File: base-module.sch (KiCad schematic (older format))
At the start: 0 parts

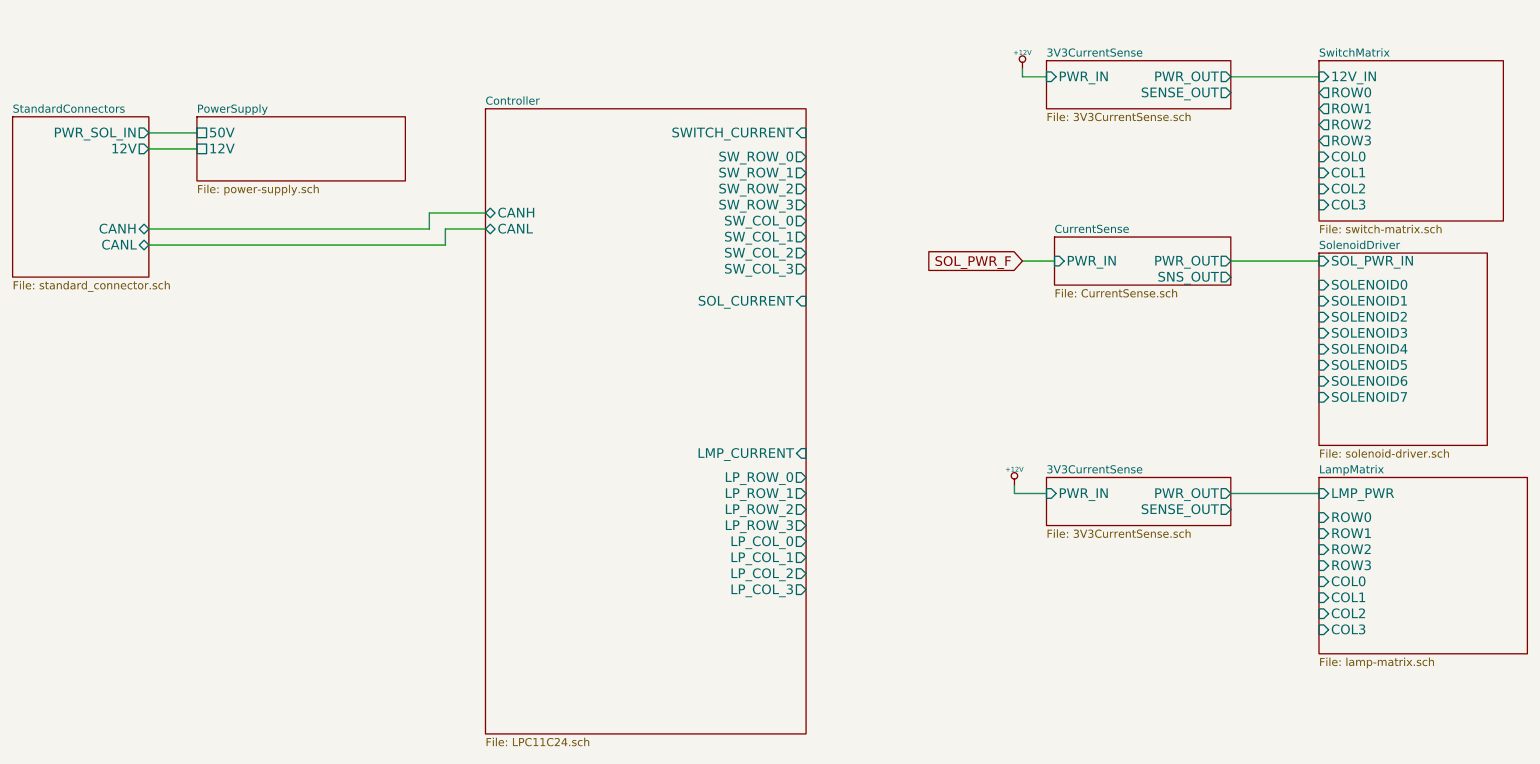
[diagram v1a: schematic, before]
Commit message: finished main controller, added LED's to power system.
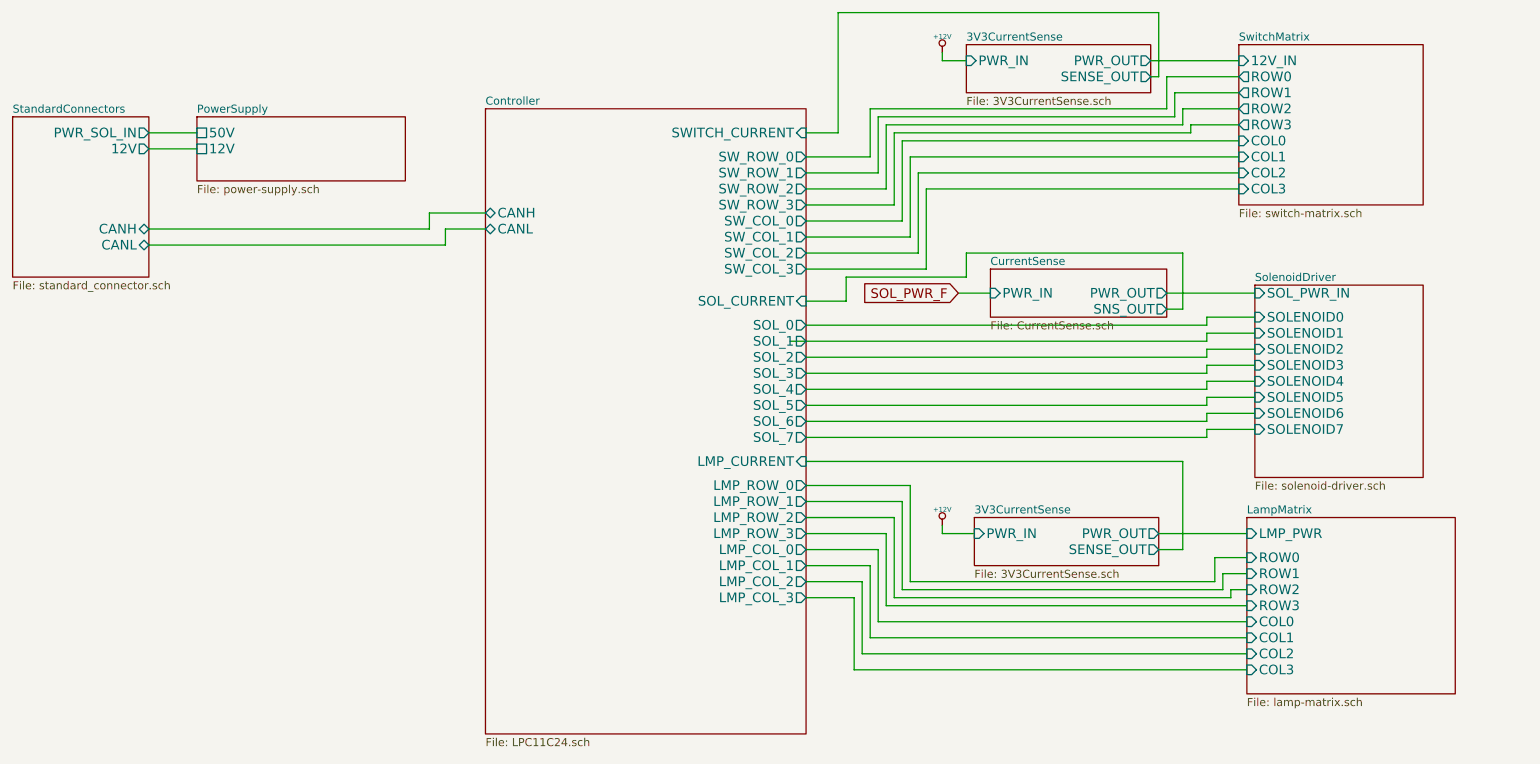
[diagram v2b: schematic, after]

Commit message: ran an ERC and touched up a couple small issues
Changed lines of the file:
@@
-EESchema Schematic File Version 2  date 4/18/2013 12:55:47 AM
+EESchema Schematic File Version 2  date 4/18/2013 1:12:38 AM
 LIBS:power
 LIBS:device
@@
 F2 "50V" U L 1750 1550 60
 F3 "12V" U L 1750 1650 60
+F4 "Power_EN" I L 1750 1750 60
 $EndSheet
 $Sheet
@@
 S 6600 3950 1150 300
 U 516D6DB7
-F0 "3V3CurrentSense" 50
-F1 "3V3CurrentSense.sch" 50
+F0 "3V3CurrentSense_2" 50
+F1 "3V3CurrentSense_2.sch" 50
 F2 "PWR_IN" I L 6600 4050 60
 F3 "PWR_OUT" O R 7750 4050 60
@@
 $EndSheet
 $Comp
-L +12V #PWR1
+L +12V #PWR01
 U 1 1 516D8357
 P 6400 4000
-F 0 "#PWR1" H 6400 3950 20  0001 C CNN
+F 0 "#PWR01" H 6400 3950 20  0001 C CNN
 F 1 "+12V" H 6400 4100 30  0000 C CNN
 F 2 "" H 6400 4000 60  0000 C CNN
@@
 $EndComp
 $Comp
-L +12V #PWR2
+L +12V #PWR02
 U 1 1 516D85FA
 P 6400 1050
-F 0 "#PWR2" H 6400 1000 20  0001 C CNN
+F 0 "#PWR02" H 6400 1000 20  0001 C CNN
 F 1 "+12V" H 6400 1150 30  0000 C CNN
 F 2 "" H 6400 1050 60  0000 C CNN
@@
 	8050 2850 8050 2800
 Wire Wire Line
-	5450 2850 8050 2850
+	5550 2850 8050 2850
 Wire Wire Line
 	8050 2750 5550 2750
